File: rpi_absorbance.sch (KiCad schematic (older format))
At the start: 13 parts, among them P1 CONN_01X05, U1 MAX6071, U2 LTC2452, U3 SD100-13-23-222, U4 OPA381

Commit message: Improve PCB layout
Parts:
- added C8: 10u, Capacitors_SMD:C_0603, symbol C_Small
- added R2: 16k, Resistors_SMD:R_0603, symbol R_Small
- C1, C2, C3, C4, C5, C6, C7: footprint Capacitors_SMD:C_0603_HandSoldering -> Capacitors_SMD:C_0603
- R1: footprint Resistors_SMD:R_0603_HandSoldering -> Resistors_SMD:R_0603
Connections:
- wire segments 66 -> 70
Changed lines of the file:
@@
 F 0 "C5" H 4610 2970 50  0000 L CNN
 F 1 "1u" H 4610 2820 50  0000 L CNN
-F 2 "Capacitors_SMD:C_0603_HandSoldering" H 4600 2900 50  0001 C CNN
+F 2 "Capacitors_SMD:C_0603" H 4600 2900 50  0001 C CNN
 F 3 "" H 4600 2900 50  0000 C CNN
 	1    4600 2900
@@
 F 0 "C3" H 4410 2970 50  0000 L CNN
 F 1 "10u" H 4410 2820 50  0000 L CNN
-F 2 "Capacitors_SMD:C_0603_HandSoldering" H 4400 2900 50  0001 C CNN
+F 2 "Capacitors_SMD:C_0603" H 4400 2900 50  0001 C CNN
 F 3 "" H 4400 2900 50  0000 C CNN
 	1    4400 2900
@@
 F 0 "C4" H 4510 3920 50  0000 L CNN
 F 1 ".1u" H 4510 3770 50  0000 L CNN
-F 2 "Capacitors_SMD:C_0603_HandSoldering" H 4500 3850 50  0001 C CNN
+F 2 "Capacitors_SMD:C_0603" H 4500 3850 50  0001 C CNN
 F 3 "" H 4500 3850 50  0000 C CNN
 	1    4500 3850
@@
 F 0 "C2" H 4010 4570 50  0000 L CNN
 F 1 ".1u" H 4010 4420 50  0000 L CNN
-F 2 "Capacitors_SMD:C_0603_HandSoldering" H 4000 4500 50  0001 C CNN
+F 2 "Capacitors_SMD:C_0603" H 4000 4500 50  0001 C CNN
 F 3 "" H 4000 4500 50  0000 C CNN
 	1    4000 4500
@@
 F 0 "C1" H 4010 4070 50  0000 L CNN
 F 1 ".1u" H 4010 3920 50  0000 L CNN
-F 2 "Capacitors_SMD:C_0603_HandSoldering" H 4000 4000 50  0001 C CNN
+F 2 "Capacitors_SMD:C_0603" H 4000 4000 50  0001 C CNN
 F 3 "" H 4000 4000 50  0000 C CNN
 	1    4000 4000
@@
 F 0 "C6" H 7010 4420 50  0000 L CNN
 F 1 ".1u" H 7010 4270 50  0000 L CNN
-F 2 "Capacitors_SMD:C_0603_HandSoldering" H 7000 4350 50  0001 C CNN
+F 2 "Capacitors_SMD:C_0603" H 7000 4350 50  0001 C CNN
 F 3 "" H 7000 4350 50  0000 C CNN
 	1    7000 4350
@@
 F 0 "C7" H 6260 4970 50  0000 L CNN
 F 1 ".5p" H 6260 4820 50  0000 L CNN
-F 2 "Capacitors_SMD:C_0603_HandSoldering" H 6250 4900 50  0001 C CNN
+F 2 "Capacitors_SMD:C_0603" H 6250 4900 50  0001 C CNN
 F 3 "" H 6250 4900 50  0000 C CNN
 	1    6250 4900
@@
 F 0 "R1" H 6280 4670 50  0000 L CNN
 F 1 "10M" H 6280 4610 50  0000 L CNN
-F 2 "Resistors_SMD:R_0603_HandSoldering" H 6250 4650 50  0001 C CNN
+F 2 "Resistors_SMD:R_0603" H 6250 4650 50  0001 C CNN
 F 3 "" H 6250 4650 50  0000 C CNN
 	1    6250 4650
@@
 Wire Wire Line
 	6650 4250 7000 4250
-Wire Wire Line
-	5600 3850 6750 3850
 Connection ~ 4400 2750
 Wire Wire Line
@@
 	5850 2500 5850 2600
 Wire Wire Line
-	6750 3850 6750 4800
+	6750 3750 6750 4800
 Wire Wire Line
 	6750 4350 6650 4350
@@
 	5350 4550 5450 4550
 Wire Wire Line
-	5600 3950 5600 4450
+	5600 4450 5600 3950
 Wire Wire Line
 	5400 4550 5400 4550
@@
 	5700 4250 5850 4250
 Wire Wire Line
-	5600 4450 5350 4450
+	5350 4450 5600 4450
 Wire Wire Line
 	5400 4450 5400 4550
@@
 Connection ~ 6750 4350
 Connection ~ 6400 4800
+$Comp
+L R_Small R2
+U 1 1 569B2F31
+P 6300 3750
+F 0 "R2" H 6330 3770 50  0000 L CNN
+F 1 "16k" H 6330 3710 50  0000 L CNN
+F 2 "Resistors_SMD:R_0603" H 6300 3750 50  0001 C CNN
+F 3 "" H 6300 3750 50  0000 C CNN
+	1    6300 3750
+	0    1    1    0
+$EndComp
+$Comp
+L C_Small C8
+U 1 1 569B2FF9
+P 6100 3650
+F 0 "C8" H 6110 3720 50  0000 L CNN
+F 1 "10u" H 6110 3570 50  0000 L CNN
+F 2 "Capacitors_SMD:C_0603" H 6100 3650 50  0001 C CNN
+F 3 "" H 6100 3650 50  0000 C CNN
+	1    6100 3650
+	-1   0    0    1
+$EndComp
+Wire Wire Line
+	6750 3750 6400 3750
+Wire Wire Line
+	6200 3750 6100 3750
+Wire Wire Line
+	6100 3750 6100 3850
+Wire Wire Line
+	6100 3850 5600 3850
+$Comp
+L GND #PWR019
+U 1 1 569B3249
+P 6100 3500
+F 0 "#PWR019" H 6100 3250 50  0001 C CNN
+F 1 "GND" H 6100 3350 50  0000 C CNN
+F 2 "" H 6100 3500 50  0000 C CNN
+F 3 "" H 6100 3500 50  0000 C CNN
+	1    6100 3500
+	-1   0    0    1
+$EndComp
+Wire Wire Line
+	6100 3500 6100 3550
 $EndSCHEMATC

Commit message: Add different ADC
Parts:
- removed P1: CONN_01X05, Pin_Headers:Pin_Header_Straight_1x05, symbol CONN_01X05
- removed U1: MAX6071, TO_SOT_Packages_SMD:SOT-23-6, symbol MAX6071
- removed U2: LTC2452, footprints:TSOT-23-8, symbol LTC2452
- added C9: 10u, Capacitors_SMD:C_0603, symbol C_Small
- added P1: CONN_01X04, Pin_Headers:Pin_Header_Straight_1x04, symbol CONN_01X04
- added U1: LTC2461, Housings_SSOP:MSOP-12_3x4mm_Pitch0.65mm, symbol LTC2461
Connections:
- net labels added: SCL, SDA
- wire segments 70 -> 67
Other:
- moved on the sheet: C8, R2

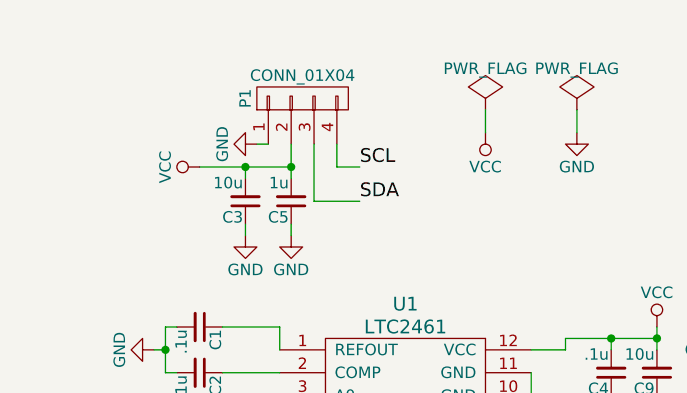
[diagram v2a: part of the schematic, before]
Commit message: Reorganize PCB
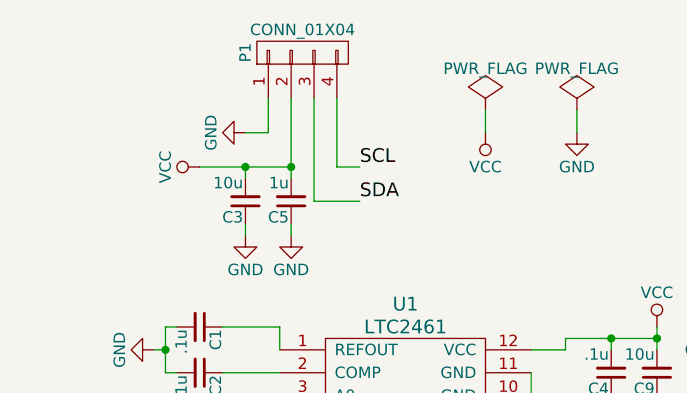
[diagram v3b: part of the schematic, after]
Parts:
- P1: footprint Pin_Headers:Pin_Header_Straight_1x04 -> footprints:CONN_1x4_SMT_2mm
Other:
- moved on the sheet: P1
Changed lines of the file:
@@
 L GND #PWR03
 U 1 1 569AE178
-P 4450 2650
-F 0 "#PWR03" H 4450 2400 50  0001 C CNN
-F 1 "GND" H 4450 2500 50  0000 C CNN
-F 2 "" H 4450 2650 50  0000 C CNN
-F 3 "" H 4450 2650 50  0000 C CNN
-	1    4450 2650
+P 4400 2600
+F 0 "#PWR03" H 4400 2350 50  0001 C CNN
+F 1 "GND" H 4400 2450 50  0000 C CNN
+F 2 "" H 4400 2600 50  0000 C CNN
+F 3 "" H 4400 2600 50  0000 C CNN
+	1    4400 2600
 	0    1    1    0
 $EndComp
@@
 $EndComp
 $Comp
-L GND #PWR020
+L GND #PWR019
 U 1 1 569C17EB
 P 4350 3850
-F 0 "#PWR020" H 4350 3600 50  0001 C CNN
+F 0 "#PWR019" H 4350 3600 50  0001 C CNN
 F 1 "GND" H 4350 3700 50  0000 C CNN
 F 2 "" H 4350 3850 50  0000 C CNN
@@
 L CONN_01X04 P1
 U 1 1 569C1ED7
-P 4650 2450
-F 0 "P1" H 4650 2700 50  0000 C CNN
-F 1 "CONN_01X04" V 4750 2450 50  0000 C CNN
-F 2 "Pin_Headers:Pin_Header_Straight_1x04" H 4650 2450 50  0001 C CNN
-F 3 "" H 4650 2450 50  0000 C CNN
-	1    4650 2450
+P 4650 2250
+F 0 "P1" H 4650 2500 50  0000 C CNN
+F 1 "CONN_01X04" V 4750 2250 50  0000 C CNN
+F 2 "footprints:CONN_1x4_SMT_2mm" H 4650 2250 50  0001 C CNN
+F 3 "" H 4650 2250 50  0000 C CNN
+	1    4650 2250
 	0    -1   -1   0
 $EndComp
@@
 	4400 3000 4400 3050
 Wire Wire Line
-	4450 2650 4500 2650
-Wire Wire Line
 	4400 2800 4400 2750
 Wire Wire Line
 	4200 2750 4600 2750
 Wire Wire Line
-	4600 2650 4600 2800
+	4600 2450 4600 2800
 Connection ~ 4600 2750
 Wire Wire Line
@@
 	4500 4200 4200 4200
 Wire Wire Line
-	4700 2650 4700 2900
+	4700 2450 4700 2900
 Wire Wire Line
 	4700 2900 4900 2900
 Wire Wire Line
-	4800 2650 4800 2750
+	4800 2450 4800 2750
 Wire Wire Line
 	4800 2750 4900 2750
@@
 Wire Wire Line
 	4550 3850 4550 3750
+Wire Wire Line
+	4400 2600 4500 2600
+Wire Wire Line
+	4500 2600 4500 2450
 $EndSCHEMATC

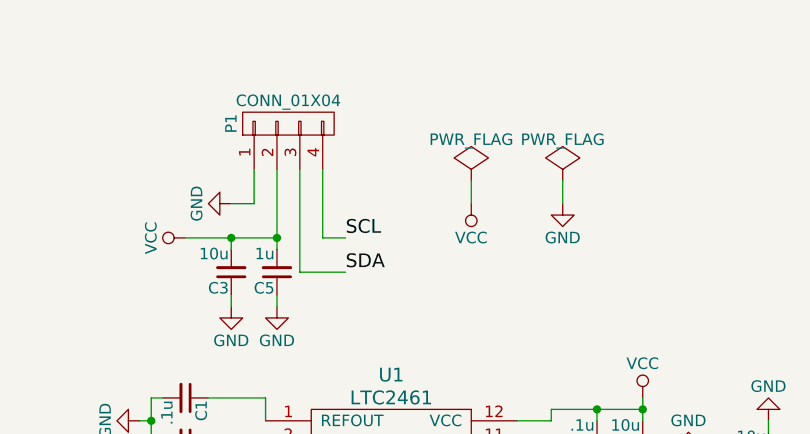
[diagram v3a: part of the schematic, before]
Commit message: Add USB AB micro connector
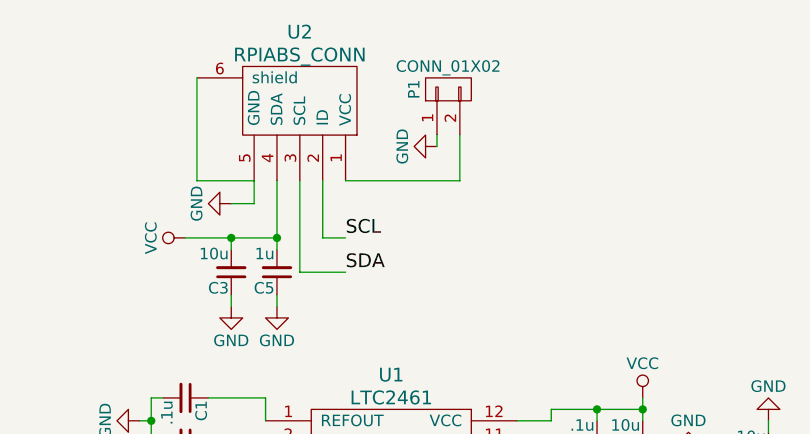
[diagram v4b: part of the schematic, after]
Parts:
- removed P1: CONN_01X04, footprints:CONN_1x4_SMT_2mm, symbol CONN_01X04
- added P1: CONN_01X02, Pin_Headers:Pin_Header_Straight_1x02, symbol CONN_01X02
- added U2: RPIABS_CONN, footprints:FCI_10104111-0001LF, symbol RPIABS_CONN
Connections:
- net GND: now also P1.1 (P1), U2.5 (GND), U2.6 (shield)
- net SCL: now also U2.2 (ID)
- net SDA: now also U2.3 (SCL)
- net VCC: now also U2.4 (SDA)
- new net: P1.2 (P2), U2.1 (VCC)

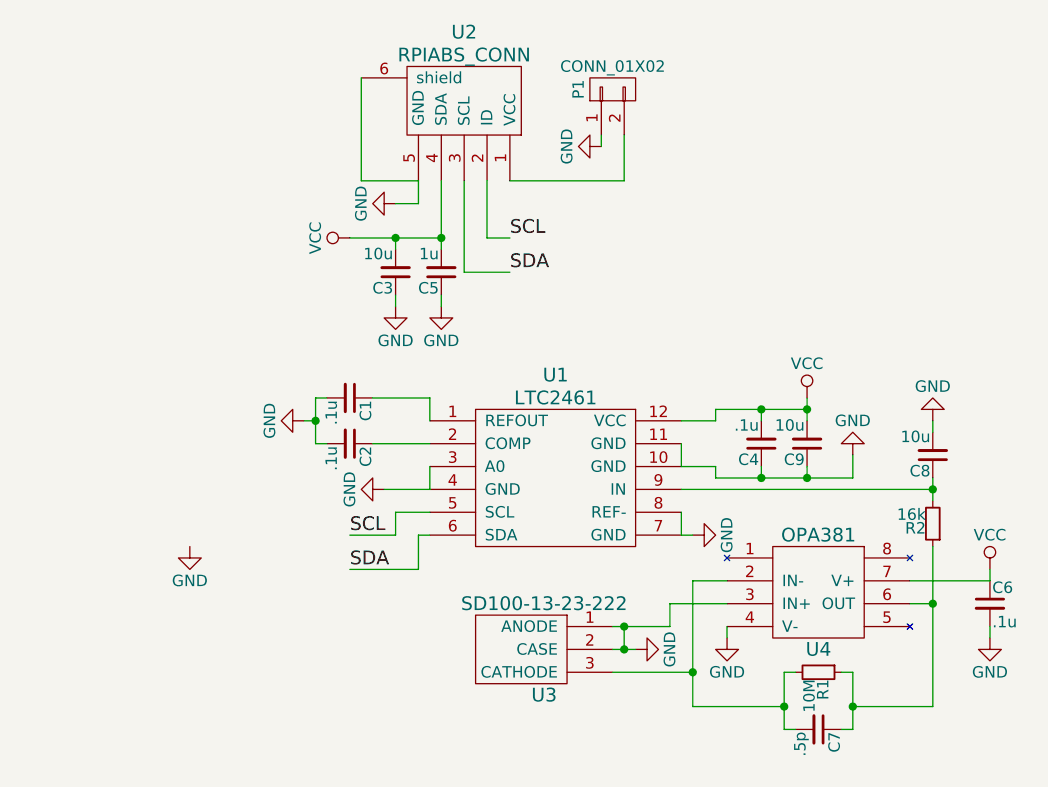
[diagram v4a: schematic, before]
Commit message: Reorganize PCB
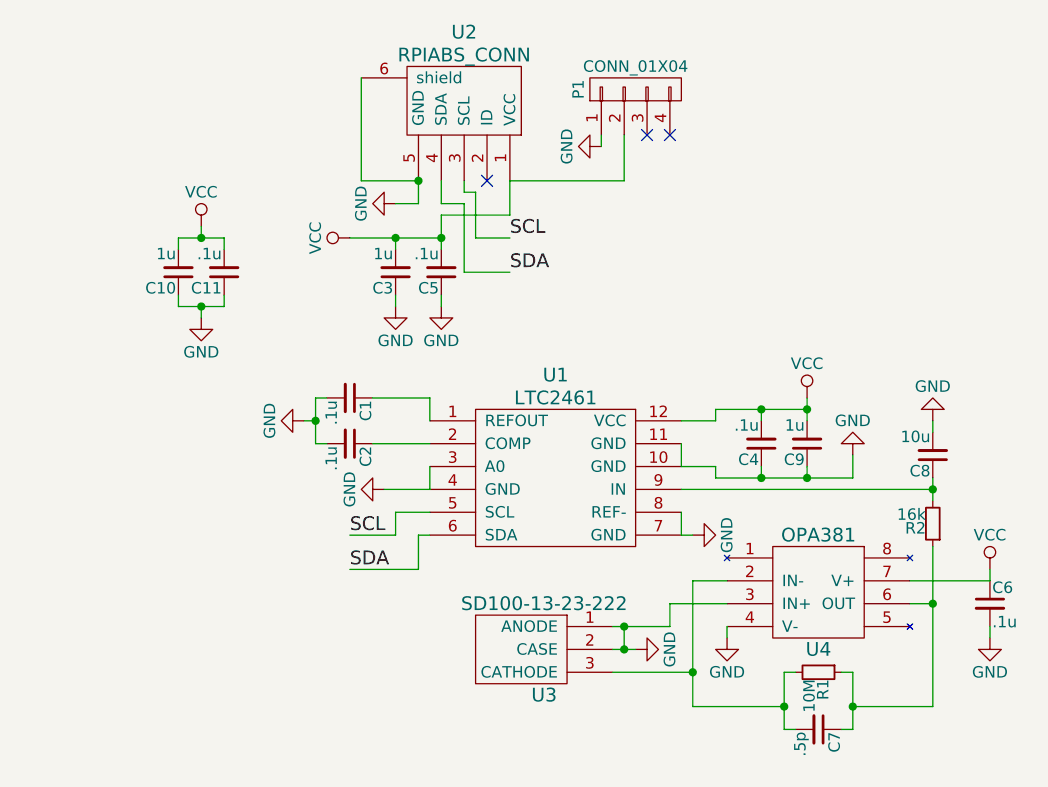
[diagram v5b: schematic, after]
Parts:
- removed P1: CONN_01X02, Pin_Headers:Pin_Header_Straight_1x02, symbol CONN_01X02
- added C10: 1u, Capacitors_SMD:C_0603, symbol C_Small
- added C11: .1u, Capacitors_SMD:C_0603, symbol C_Small
- added P1: CONN_01X04, footprints:Hirose_DF13-4P-1.25V(20), symbol CONN_01X04
- C3, C9: value 10u -> 1u
- C5: value 1u -> .1u
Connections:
- net GND: now also C10.1, C11.1, P1.1 (P1)
- net SCL: now also U2.3 (SCL); no longer U2.2 (ID)
- net SDA: now also U2.4 (SDA); no longer U2.3 (SCL)
- net VCC: now also U2.1 (VCC), C10.2, C11.2, P1.2 (P2); no longer U2.4 (SDA)
- no-connect marks 0 -> 3
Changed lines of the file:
@@
 P 4600 2900
 F 0 "C5" H 4610 2970 50  0000 L CNN
-F 1 "1u" H 4610 2820 50  0000 L CNN
+F 1 ".1u" H 4610 2820 50  0000 L CNN
 F 2 "Capacitors_SMD:C_0603" H 4600 2900 50  0001 C CNN
 F 3 "" H 4600 2900 50  0000 C CNN
@@
 P 4400 2900
 F 0 "C3" H 4410 2970 50  0000 L CNN
-F 1 "10u" H 4410 2820 50  0000 L CNN
+F 1 "1u" H 4410 2820 50  0000 L CNN
 F 2 "Capacitors_SMD:C_0603" H 4400 2900 50  0001 C CNN
 F 3 "" H 4400 2900 50  0000 C CNN
@@
 P 6200 3650
 F 0 "C9" H 6210 3720 50  0000 L CNN
-F 1 "10u" H 6210 3570 50  0000 L CNN
+F 1 "1u" H 6210 3570 50  0000 L CNN
 F 2 "Capacitors_SMD:C_0603" H 6200 3650 50  0001 C CNN
 F 3 "" H 6200 3650 50  0000 C CNN
@@
 $EndComp
 $Comp
-L GND #PWR013
-U 1 1 569C12C5
-P 3500 4100
-F 0 "#PWR013" H 3500 3850 50  0001 C CNN
-F 1 "GND" H 3500 3950 50  0000 C CNN
-F 2 "" H 3500 4100 50  0000 C CNN
-F 3 "" H 3500 4100 50  0000 C CNN
-	1    3500 4100
-	1    0    0    -1
-$EndComp
-$Comp
-L VCC #PWR014
+L VCC #PWR013
 U 1 1 569C1370
 P 6200 3450
-F 0 "#PWR014" H 6200 3300 50  0001 C CNN
+F 0 "#PWR013" H 6200 3300 50  0001 C CNN
 F 1 "VCC" H 6200 3600 50  0000 C CNN
 F 2 "" H 6200 3450 50  0000 C CNN
@@
 $EndComp
 $Comp
-L GND #PWR015
+L GND #PWR014
 U 1 1 569C17EB
 P 4350 3850
-F 0 "#PWR015" H 4350 3600 50  0001 C CNN
+F 0 "#PWR014" H 4350 3600 50  0001 C CNN
 F 1 "GND" H 4350 3700 50  0000 C CNN
 F 2 "" H 4350 3850 50  0000 C CNN
@@
 	4350 3850 4550 3850
 Wire Wire Line
-	4800 2750 4900 2750
+	4750 2750 4900 2750
 Wire Wire Line
 	4700 2900 4900 2900
@@
 $EndComp
 Wire Wire Line
-	4600 2500 4600 2800
-Wire Wire Line
-	4700 2900 4700 2500
-Wire Wire Line
-	4800 2750 4800 2500
-Wire Wire Line
 	4250 2050 4250 2500
 Wire Wire Line
-	4250 2500 4500 2500
-$Comp
-L CONN_01X02 P1
-U 1 1 56A00E7A
-P 5350 2100
-F 0 "P1" H 5350 2250 50  0000 C CNN
-F 1 "CONN_01X02" V 5450 2100 50  0000 C CNN
-F 2 "Pin_Headers:Pin_Header_Straight_1x02" H 5350 2100 50  0001 C CNN
-F 3 "" H 5350 2100 50  0000 C CNN
-	1    5350 2100
-	0    -1   -1   0
-$EndComp
-Wire Wire Line
 	4900 2500 5400 2500
 Wire Wire Line
 	5400 2500 5400 2300
 $Comp
-L GND #PWR016
+L GND #PWR015
 U 1 1 56A00F92
 P 5300 2350
-F 0 "#PWR016" H 5300 2100 50  0001 C CNN
+F 0 "#PWR015" H 5300 2100 50  0001 C CNN
 F 1 "GND" H 5300 2200 50  0000 C CNN
 F 2 "" H 5300 2350 50  0000 C CNN
@@
 Wire Wire Line
 	5300 2350 5300 2300
+$Comp
+L CONN_01X04 P1
+U 1 1 56A52DAF
+P 5450 2100
+F 0 "P1" H 5450 2350 50  0000 C CNN
+F 1 "CONN_01X04" V 5550 2100 50  0000 C CNN
+F 2 "footprints:Hirose_DF13-4P-1.25V(20)" H 5450 2100 50  0001 C CNN
+F 3 "" H 5450 2100 50  0000 C CNN
+	1    5450 2100
+	0    -1   -1   0
+$EndComp
+Wire Wire Line
+	4700 2900 4700 2600
+Wire Wire Line
+	4700 2600 4600 2600
+Wire Wire Line
+	4600 2600 4600 2500
+Wire Wire Line
+	4750 2750 4750 2550
+Wire Wire Line
+	4750 2550 4700 2550
+Wire Wire Line
+	4700 2550 4700 2500
+Wire Wire Line
+	4600 2650 4600 2800
+Wire Wire Line
+	4600 2650 4900 2650
+Wire Wire Line
+	4900 2650 4900 2500
+NoConn ~ 5500 2300
+NoConn ~ 5600 2300
+Connection ~ 4500 2500
+$Comp
+L C_Small C10
+U 1 1 56A55EED
+P 3450 2900
+F 0 "C10" H 3460 2970 50  0000 L CNN
+F 1 "1u" H 3460 2820 50  0000 L CNN
+F 2 "Capacitors_SMD:C_0603" H 3450 2900 50  0001 C CNN
+F 3 "" H 3450 2900 50  0000 C CNN
+	1    3450 2900
+	-1   0    0    1
+$EndComp
+$Comp
+L C_Small C11
+U 1 1 56A55F64
+P 3650 2900
+F 0 "C11" H 3660 2970 50  0000 L CNN
+F 1 ".1u" H 3660 2820 50  0000 L CNN
+F 2 "Capacitors_SMD:C_0603" H 3650 2900 50  0001 C CNN
+F 3 "" H 3650 2900 50  0000 C CNN
+	1    3650 2900
+	-1   0    0    1
+$EndComp
+Wire Wire Line
+	3450 2800 3450 2750
+Wire Wire Line
+	3450 2750 3650 2750
+Wire Wire Line
+	3650 2750 3650 2800
+$Comp
+L VCC #PWR016
+U 1 1 56A56088
+P 3550 2700
+F 0 "#PWR016" H 3550 2550 50  0001 C CNN
+F 1 "VCC" H 3550 2850 50  0000 C CNN
+F 2 "" H 3550 2700 50  0000 C CNN
+F 3 "" H 3550 2700 50  0000 C CNN
+	1    3550 2700
+	1    0    0    -1
+$EndComp
+Wire Wire Line
+	3550 2700 3550 2750
+Connection ~ 3550 2750
+Wire Wire Line
+	3450 3000 3450 3050
+Wire Wire Line
+	3450 3050 3650 3050
+Wire Wire Line
+	3650 3050 3650 3000
+$Comp
+L GND #PWR017
+U 1 1 56A561B1
+P 3550 3100
+F 0 "#PWR017" H 3550 2850 50  0001 C CNN
+F 1 "GND" H 3550 2950 50  0000 C CNN
+F 2 "" H 3550 3100 50  0000 C CNN
+F 3 "" H 3550 3100 50  0000 C CNN
+	1    3550 3100
+	1    0    0    -1
+$EndComp
+Wire Wire Line
+	3550 3100 3550 3050
+Connection ~ 3550 3050
+Wire Wire Line
+	4250 2500 4500 2500
+NoConn ~ 4800 2500
 $EndSCHEMATC

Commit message: Add power planes
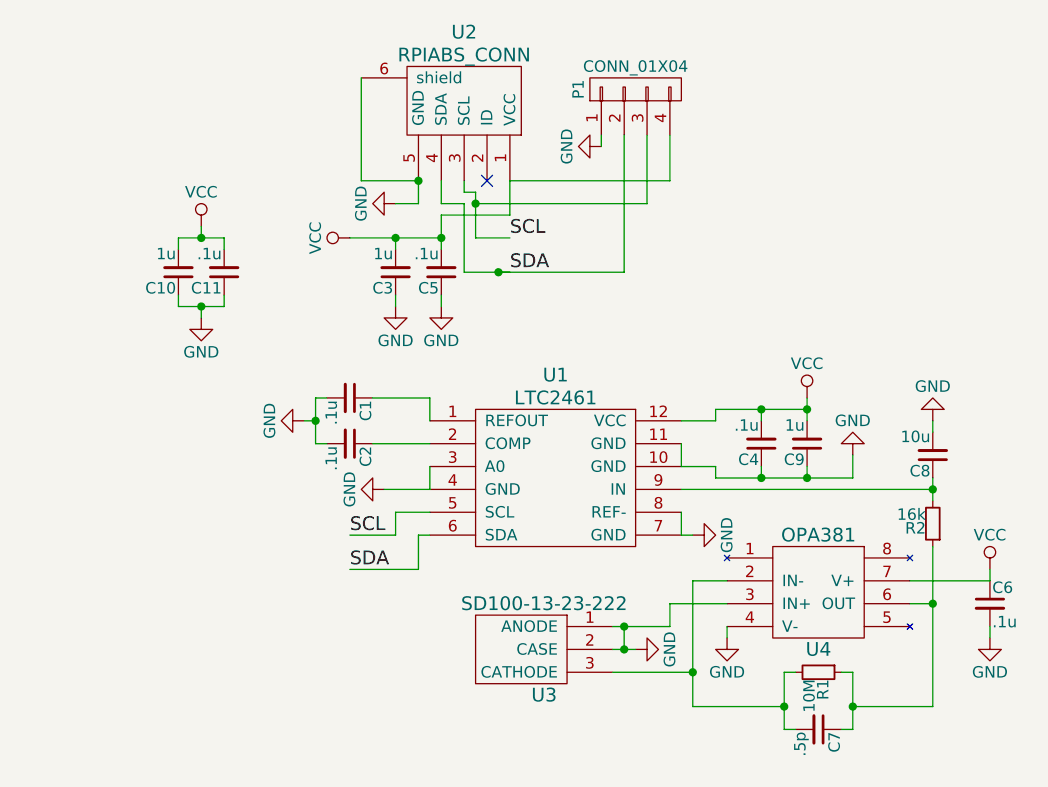
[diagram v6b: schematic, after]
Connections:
- net SCL: now also P1.3 (P3)
- net SDA: now also P1.2 (P2)
- net VCC: now also P1.4 (P4); no longer P1.2 (P2)
- no-connect marks 3 -> 1
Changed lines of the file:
@@
 	4250 2050 4250 2500
 Wire Wire Line
-	4900 2500 5400 2500
-Wire Wire Line
-	5400 2500 5400 2300
+	4900 2500 5600 2500
 $Comp
 L GND #PWR015
@@
 Wire Wire Line
 	4900 2650 4900 2500
-NoConn ~ 5500 2300
-NoConn ~ 5600 2300
 Connection ~ 4500 2500
 $Comp
@@
 	4250 2500 4500 2500
 NoConn ~ 4800 2500
+Wire Wire Line
+	5600 2500 5600 2300
+Wire Wire Line
+	4750 2600 5500 2600
+Wire Wire Line
+	5500 2600 5500 2300
+Connection ~ 4750 2600
+Wire Wire Line
+	4850 2900 5400 2900
+Wire Wire Line
+	5400 2900 5400 2300
+Connection ~ 4850 2900
 $EndSCHEMATC
